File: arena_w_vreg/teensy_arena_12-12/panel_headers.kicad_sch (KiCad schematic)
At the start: 12 parts, among them P1 CONN15, P2 CONN15, P3 CONN15, P4 CONN15, P5 CONN15, P6 CONN15

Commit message: Worked on 12-12 teensy arena with voltage regulator.
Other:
- moved on the sheet: P1, P2, P3, P4, P5, P6

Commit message: Worked on 12-12 teensy arean with voltage regulators.
Moved MOSFET to panel headers sheet. Added RESET to level sifters. Added
decouple caps for TXB0108's.
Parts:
- added Q2: MOSFET_NCHAN, Package_TO_SOT_SMD:SOT-23-3, symbol arena_custom:MOSFET_NCHAN
- added R1: 200, Resistor_SMD:R_0805_2012Metric, symbol Device:R
- added R2: 20k, Resistor_SMD:R_0805_2012Metric, symbol Device:R
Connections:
- net GND: now also Q2.2 (S), R2.1
- net PAN5V.RESET: now also R1.2; no longer P1.3, P1.3, P2.3, P2.3, P3.3, P3.3, P4.3, P4.3, P5.3, P5.3, P6.3, P6.3
- new net: Q2.1 (G), R1.1, R2.2
- new net RESET: P1.3, P1.3, P2.3, P2.3, P3.3, P3.3, P4.3, P4.3, P5.3, P5.3, P6.3, P6.3, Q2.3 (D)
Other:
- note added: "1. Double check MOSET PINOUT!!! 2. Maybe add small resistor to RESET line to limit current."
- note added: "Reset Sink"
- note added: "SI2302-TP (Digikey SI2302-TPMSCT-ND)"
- moved on the sheet: P1, P2, P3, P4, P5, P6

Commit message: Completed initial schematic for 12-12 teensy arena.
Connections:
- removed net +5V: P1.1, P1.1, P2.1, P2.1, P3.1, P3.1, P4.1, P4.1, P5.1, P5.1, P6.1, P6.1
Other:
- moved on the sheet: P1, P2, P3, P4, P5, P6, Q2, R1, R2

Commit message: Wored on teensy arena.
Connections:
- net POW.5V_HDR_5: now reaches P5.1
- net POW.5V_HDR_4: now reaches P4.1
- net POW.5V_HDR_11: now reaches P5.1
- net POW.5V_HDR_9: now reaches P3.1
- net POW.5V_HDR_6: now reaches P6.1
- net POW.5V_HDR_12: now reaches P6.1
- net POW.5V_HDR_1: now reaches P1.1
- net POW.5V_HDR_8: now reaches P2.1
- net POW.5V_HDR_3: now reaches P3.1
- net POW.5V_HDR_2: now reaches P2.1
- net POW.5V_HDR_7: now reaches P1.1
- net POW.5V_HDR_10: now reaches P4.1
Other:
- note added: "1. Check that MOSFET still required when using TXB0108 2. Add small resistor to RESET line to limit current?"
- note removed: "1. Double check MOSET PINOUT!!! 2. Maybe add small resistor to RESET line to limit current."
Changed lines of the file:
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@@
     (effects (font (size 5.08 5.08) (thickness 0.508) bold) (justify left bottom))
   )
-  (text "1. Double check MOSET PINOUT!!!\n2. Maybe add small resistor to RESET line to limit current. "
-    (at 33.02 128.905 0)
+  (text "1. Check that MOSFET still required when using TXB0108\n2. Add small resistor to RESET line to limit current?"
+    (at 28.448 134.62 0)
     (effects (font (size 2.54 2.54)) (justify left bottom))
   )
@@
     (effects (font (size 1.27 1.27)) (justify left bottom))
   )
+  (label "POW.5V_HDR_8" (at 433.832 70.485 0) (fields_autoplaced)
+    (effects (font (size 1.27 1.27)) (justify left bottom))
+  )
   (label "RESET" (at 217.678 75.565 0) (fields_autoplaced)
     (effects (font (size 1.27 1.27)) (justify left bottom))
   )
   (label "PAN5V.EXT_INT" (at 433.959 106.045 0) (fields_autoplaced)
+    (effects (font (size 1.27 1.27)) (justify left bottom))
+  )
+  (label "POW.5V_HDR_12" (at 607.822 70.485 0) (fields_autoplaced)
     (effects (font (size 1.27 1.27)) (justify left bottom))
   )
@@
     (effects (font (size 1.27 1.27)) (justify right bottom))
   )
+  (label "POW.5V_HDR_10" (at 522.732 70.485 0) (fields_autoplaced)
+    (effects (font (size 1.27 1.27)) (justify left bottom))
+  )
   (label "PAN5V.EXT_INT" (at 347.345 106.045 0) (fields_autoplaced)
     (effects (font (size 1.27 1.27)) (justify left bottom))
@@
     (effects (font (size 1.27 1.27)) (justify left bottom))
   )
+  (label "POW.5V_HDR_4" (at 262.128 70.485 0) (fields_autoplaced)
+    (effects (font (size 1.27 1.27)) (justify left bottom))
+  )
   (label "PAN5V.CS_12" (at 478.282 90.805 0) (fields_autoplaced)
     (effects (font (size 1.27 1.27)) (justify left bottom))
@@
     (effects (font (size 1.27 1.27)) (justify left bottom))
   )
+  (label "POW.5V_HDR_7" (at 389.382 70.485 0) (fields_autoplaced)
+    (effects (font (size 1.27 1.27)) (justify left bottom))
+  )
   (label "PAN5V.CS_10" (at 217.678 85.725 0) (fields_autoplaced)
     (effects (font (size 1.27 1.27)) (justify left bottom))
@@
     (effects (font (size 1.27 1.27)) (justify left bottom))
   )
+  (label "POW.5V_HDR_2" (at 173.355 70.485 0) (fields_autoplaced)
+    (effects (font (size 1.27 1.27)) (justify left bottom))
+  )
   (label "PAN5V.MOSI_0" (at 217.678 80.645 0) (fields_autoplaced)
+    (effects (font (size 1.27 1.27)) (justify left bottom))
+  )
+  (label "POW.5V_HDR_1" (at 129.032 70.485 0) (fields_autoplaced)
     (effects (font (size 1.27 1.27)) (justify left bottom))
   )
@@
     (effects (font (size 1.27 1.27)) (justify left bottom))
   )
+  (label "POW.5V_HDR_3" (at 217.678 70.485 0) (fields_autoplaced)
+    (effects (font (size 1.27 1.27)) (justify left bottom))
+  )
   (label "PAN5V.CS_05" (at 173.228 85.725 0) (fields_autoplaced)
     (effects (font (size 1.27 1.27)) (justify left bottom))
@@
     (effects (font (size 1.27 1.27)) (justify left bottom))
   )
+  (label "POW.5V_HDR_6" (at 347.218 70.485 0) (fields_autoplaced)
+    (effects (font (size 1.27 1.27)) (justify left bottom))
+  )
   (label "PAN5V.MISO_1" (at 433.832 83.185 0) (fields_autoplaced)
     (effects (font (size 1.27 1.27)) (justify left bottom))
@@
     (effects (font (size 1.27 1.27)) (justify left bottom))
   )
+  (label "POW.5V_HDR_11" (at 565.912 70.485 0) (fields_autoplaced)
+    (effects (font (size 1.27 1.27)) (justify left bottom))
+  )
   (label "PAN5V.MISO_1" (at 522.732 83.185 0) (fields_autoplaced)
     (effects (font (size 1.27 1.27)) (justify left bottom))
@@
     (effects (font (size 1.27 1.27)) (justify left bottom))
   )
+  (label "POW.5V_HDR_9" (at 478.282 70.485 0) (fields_autoplaced)
+    (effects (font (size 1.27 1.27)) (justify left bottom))
+  )
   (label "PAN5V.SCK_1" (at 478.282 78.105 0) (fields_autoplaced)
     (effects (font (size 1.27 1.27)) (justify left bottom))
@@
     (effects (font (size 1.27 1.27)) (justify left bottom))
   )
+  (label "POW.5V_HDR_5" (at 305.308 70.485 0) (fields_autoplaced)
+    (effects (font (size 1.27 1.27)) (justify left bottom))
+  )

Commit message: Worked on 12-12 schematic & part selection.
Added new 5A regulators. Added load resistors so that regulators
always have minimum load.
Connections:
- net RESET is gone; now on net PAN5V.SCK_1: P1.3, P1.3, P2.3, P2.3, P3.3, P3.3, P4.3, P4.3, P5.3, P5.3, P6.3, P6.3, Q2.3 (D)
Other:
- note added: "SI2302-TP Digikey SI2302-TPMSCT-ND LCSC C4748714 Check footprint & pinout!!!"
- note removed: "1. Check that MOSFET still required when using TXB0108 2. Add small resistor to RESET line to limit current?"
- note removed: "Reset Sink"
- note removed: "SI2302-TP (Digikey SI2302-TPMSCT-ND)"

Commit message: Worked on routing 12-12 arena with vreg.
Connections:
- net PAN5V.SCK_1: no longer P1.3, P1.3, P2.3, P2.3, P3.3, P3.3, P4.3, P4.3, P5.3, P5.3, P6.3, P6.3, Q2.3 (D)
- new net RESET: P1.3, P1.3, P2.3, P2.3, P3.3, P3.3, P4.3, P4.3, P5.3, P5.3, P6.3, P6.3, Q2.3 (D)

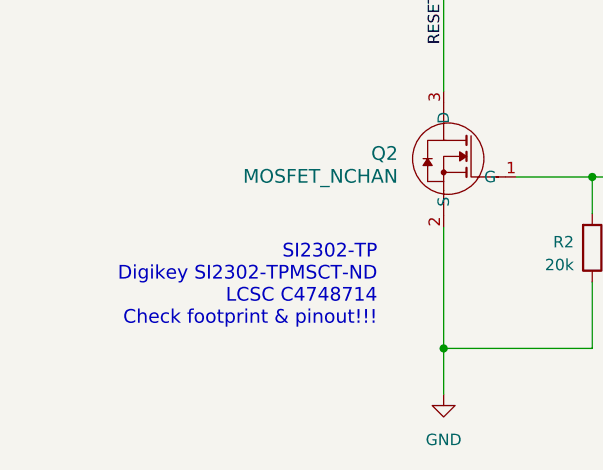
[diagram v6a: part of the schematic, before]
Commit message: Removed old notes from schematic pdf.
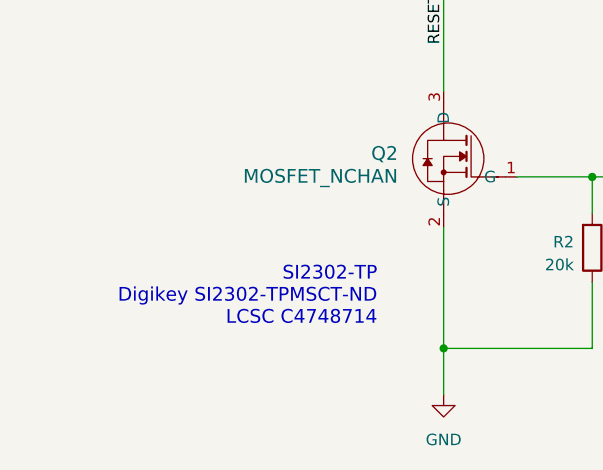
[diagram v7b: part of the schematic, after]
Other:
- note added: "SI2302-TP Digikey SI2302-TPMSCT-ND LCSC C4748714"
- note removed: "SI2302-TP Digikey SI2302-TPMSCT-ND LCSC C4748714 Check footprint & pinout!!!"
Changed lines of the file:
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@@
     (effects (font (size 5.08 5.08) (thickness 0.508) bold) (justify left bottom))
   )
-  (text "SI2302-TP \nDigikey SI2302-TPMSCT-ND\nLCSC C4748714  \nCheck footprint & pinout!!!"
+  (text "SI2302-TP \nDigikey SI2302-TPMSCT-ND\nLCSC C4748714  \n"
     (at 55.245 107.061 0)
     (effects (font (size 1.524 1.524)) (justify right bottom))
